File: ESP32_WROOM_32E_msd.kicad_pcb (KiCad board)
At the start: 2 copper layers, 49.5 x 74 mm, 21 parts, among them J1 XH_6pin, J2 XH_6pin, J3 XH_2pin, J4 XH_2pin, SW1 SW_SPDT, U2 MCP2561-E-SN

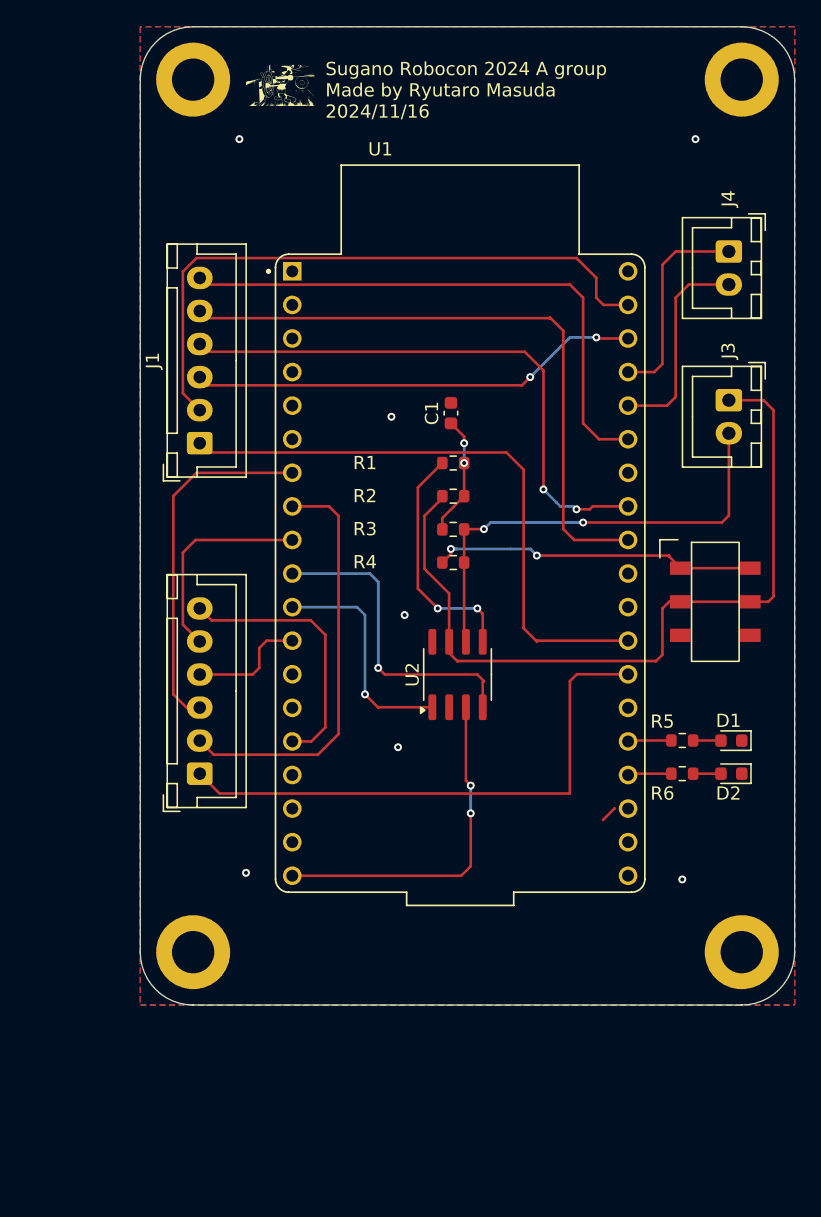
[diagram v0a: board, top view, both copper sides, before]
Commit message: change switch
because no stock on JLCPCB
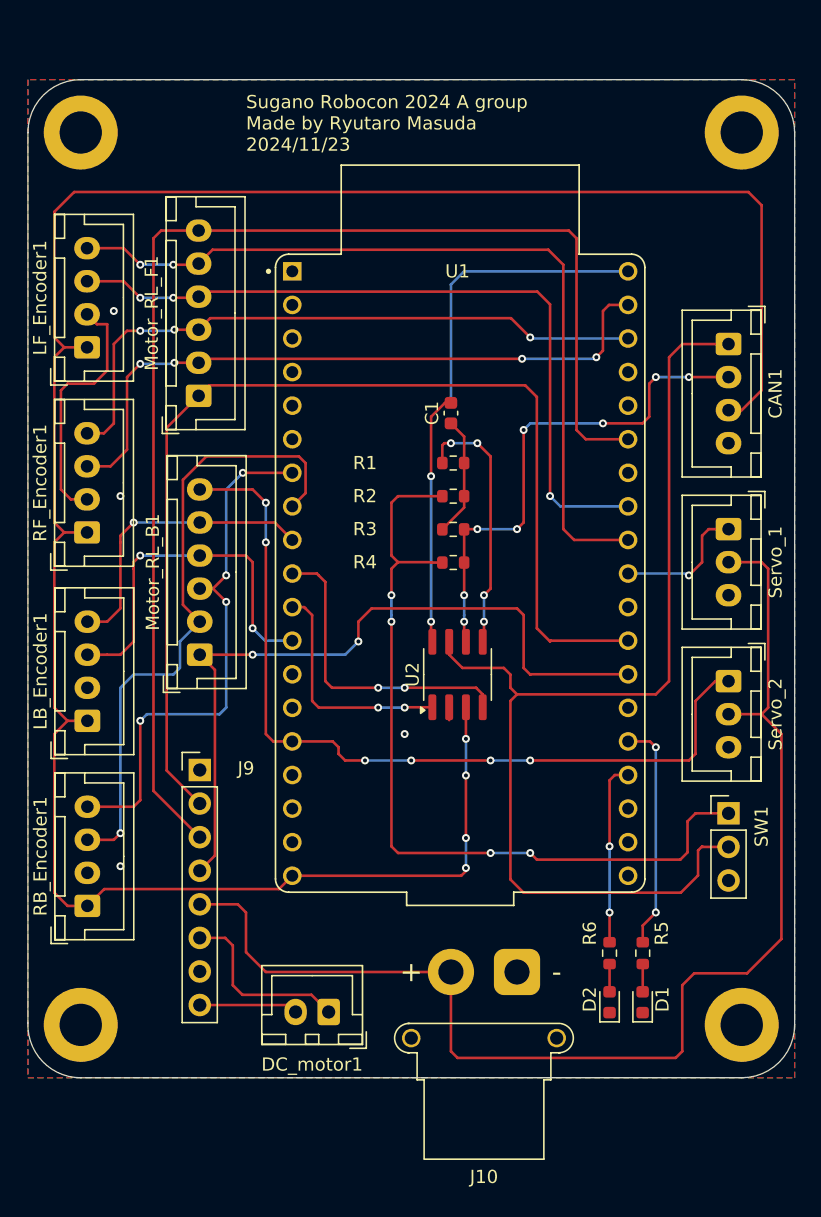
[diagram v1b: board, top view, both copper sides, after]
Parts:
- removed G***: LOGO, my_library:mickey
- removed J3, J4: XH_2pin, Connector_JST:JST_XH_B2B-XH-A_1x02_P2.50mm_Vertical
- added CAN1: CAN_External_Pin, Connector_JST:JST_XH_B4B-XH-A_1x04_P2.50mm_Vertical, F.Cu at (130.5, 61.0)
- added DC_motor1: DC_Motor, Connector_JST:JST_XH_B2B-XH-A_1x02_P2.50mm_Vertical, F.Cu at (100.2, 111.5)
- added J10: 7.5V, Connector_AMASS:AMASS_XT30PW-F_1x02_P2.50mm_Horizontal, F.Cu at (114.5, 108.5)
- added J9: Motor_Driver, Connector_PinHeader_2.54mm:PinHeader_1x08_P2.54mm_Vertical, F.Cu at (90.5, 93.2)
- added LB_Encoder1: LB_Encoder, Connector_JST:JST_XH_B4B-XH-A_1x04_P2.50mm_Vertical, F.Cu at (82.0, 89.5)
- added LF_Encoder1: LF_Encoder, Connector_JST:JST_XH_B4B-XH-A_1x04_P2.50mm_Vertical, F.Cu at (82.0, 61.2)
- added RB_Encoder1: RB_Encoder, Connector_JST:JST_XH_B4B-XH-A_1x04_P2.50mm_Vertical, F.Cu at (82.0, 103.5)
- added RF_Encoder1: RF_Encoder, Connector_JST:JST_XH_B4B-XH-A_1x04_P2.50mm_Vertical, F.Cu at (82.0, 75.2)
- added Servo_1: Servo_1, Connector_JST:JST_XH_B3B-XH-A_1x03_P2.50mm_Vertical, F.Cu at (130.5, 75.0)
- added Servo_2: Servo_2, Connector_JST:JST_XH_B3B-XH-A_1x03_P2.50mm_Vertical, F.Cu at (130.5, 86.5)
- Motor_RL_B1: renamed from J2; value XH_6pin -> Motor_RL_B
- Motor_RL_F1: renamed from J1; value XH_6pin -> Motor_RL_F
- SW1: footprint Original:slide_SW -> Connector_PinHeader_2.54mm:PinHeader_1x03_P2.54mm_Vertical
- moved D1 20.9 mm to (124.0, 110.8), turned to 90 degrees
- moved D2 19.6 mm to (121.5, 110.8), turned to 90 degrees
- moved R5 16.4 mm to (124.0, 107.1), turned to -90 degrees
- moved SW1 16.0 mm to (130.5, 96.5)
- moved R6 14.6 mm to (121.5, 107.1), turned to -90 degrees
- moved H1 10.1 mm to (81.5, 112.5)
- moved H3 9.39 mm to (81.5, 45.0)
- moved Motor_RL_B1 9.00 mm to (90.5, 84.5)
- moved H2 5.50 mm to (131.5, 112.5)
- moved H4 4.00 mm to (131.5, 45.0)
- moved Motor_RL_F1 3.58 mm to (90.4, 64.9)
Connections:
- H1 pad 1: GND -> unconnected-(H1-Pad1)
- H2 pad 1: GND -> unconnected-(H2-Pad1)
- H3 pad 1: GND -> unconnected-(H3-Pad1)
- H4 pad 1: GND -> unconnected-(H4-Pad1)
- R2 pad 1: CAN_H -> Net-(SW1-A)
- U1 pad J3_10: unconnected-(U1-IO5-PadJ3_10) -> Servo1
- U1 pad J3_4: UART_TX -> unconnected-(U1-TXD0-PadJ3_4)
- U1 pad J3_5: UART_RX -> unconnected-(U1-RXD0-PadJ3_5)
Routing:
- net +5V: track 26.0 -> 175.2 mm, vias 2 -> 4
- net +7.5V: track 0.00 -> 95.3 mm
- net GND: track 0.00 -> 62.9 mm, vias 7 -> 6
- net LF_PWM: track 43.0 -> 97.9 mm
- net LB_PWM: track 20.3 -> 63.9 mm, vias 0 -> 6
- net RF_PWM: track 45.7 -> 84.0 mm
- net Net-(SW1-A): track 25.1 -> 62.6 mm, vias 2 -> 4
- net CAN_H: track 57.8 -> 83.0 mm
- net LB_2: track 8.94 -> 27.7 mm, vias 0 -> 2
- net RB_2: track 31.9 -> 48.1 mm, vias 0 -> 1
- net UART_RX: track 15.8 -> 0.00 mm
- net UART_TX: track 15.8 -> 0.00 mm
- net RB_PWM: track 41.7 -> 56.4 mm, vias 0 -> 2
- net RF_1: track 34.2 -> 48.7 mm, vias 2 -> 3
- net LF_1: track 48.4 -> 62.7 mm, vias 0 -> 2
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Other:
- board size 49.5 x 74 mm -> 58 x 75.5 mm
- board text added: "Sugano Robocon 2024 A group Made by Ryutaro Masuda 2024/11/23"
- board text removed: "Sugano Robocon 2024 A group Made by Ryutaro Masuda 2024/11/16"
